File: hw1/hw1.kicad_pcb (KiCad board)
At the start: 2 copper layers, 68.6 x 53.3 mm, 28 parts, among them J1 CONN_01X06, P1 Power, P10 CONTROL, P2 Analog, P3 Digital, P4 Digital, P5 CONN_01X01, P6 CONN_01X01, P7 CONN_01X01, P8 CONN_01X01, P9 FX2LA, U1 STM32L151C6TxA, U2 MIC550x-3.3YM5, Y1 Crystal_GND24_Small

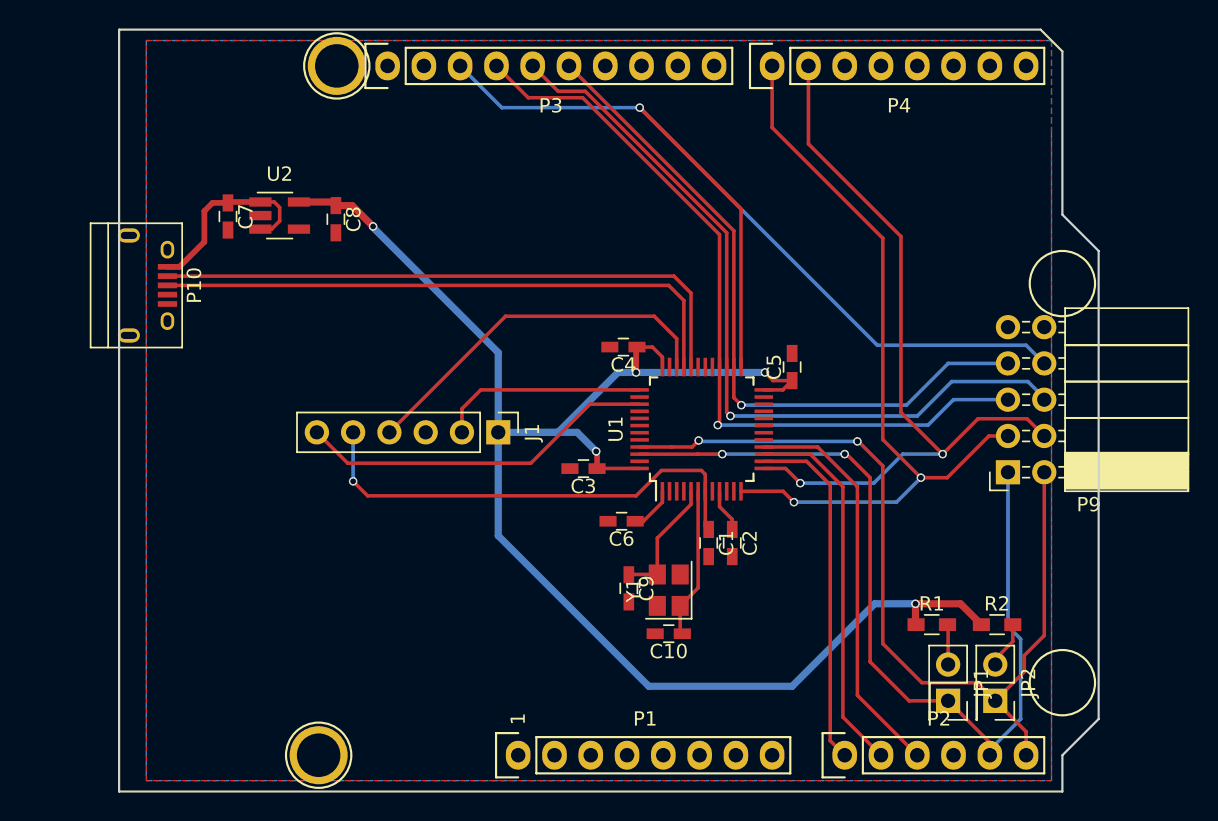
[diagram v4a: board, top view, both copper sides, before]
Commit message: "fix" grounds by tracks into pour
"finish" routing, ignore DRC violations from disconnected usb shield on
pin 6.

Add boot0 jumper pad "just in case" but really kinda dumb, we've got a
debug header on it. Why bother with this?

Change paper size in schema to get more space.

TODO: add silk?
TODO: replace "arduino" shape with just the pinpoints.
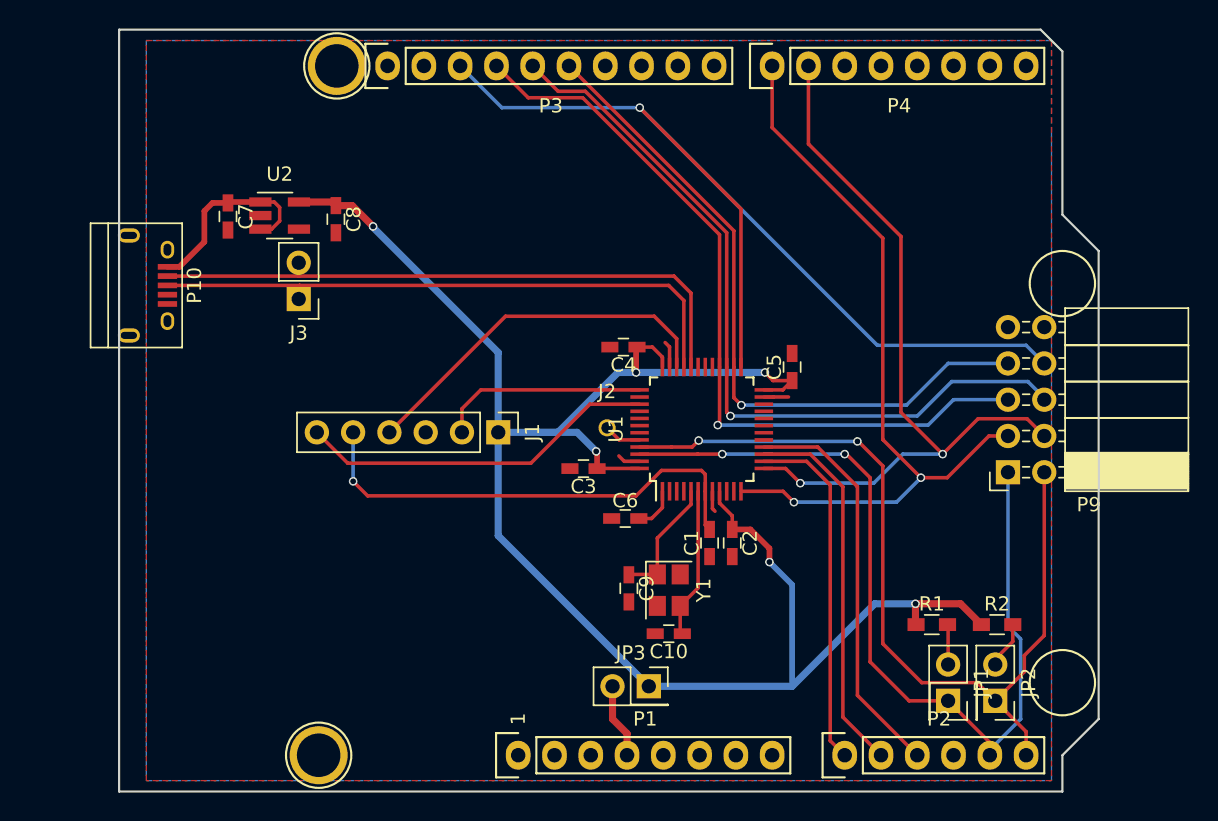
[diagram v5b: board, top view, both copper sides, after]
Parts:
- added J2: CONN_01X01_MALE, Wire_Pads:SolderWirePad_single_0-8mmDrill, F.Cu at (145.2, 100.9)
- added J3: CONN_01X02, Pin_Headers:Pin_Header_Straight_1x02_Pitch2.54mm, F.Cu at (123.6, 91.9)
- added JP3: Jumper_NC_Small, Socket_Strips:Socket_Strip_Straight_2x01_Pitch2.54mm, F.Cu at (148.1, 119.0)
- moved C6 0.32 mm to (146.4, 107.3), turned to 0 degrees
- moved C1 0.06 mm to (152.3, 109.0), turned to 90 degrees
- turned Y1 to 270 degrees
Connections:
- C1 pad 1: /NRST -> GND
- C1 pad 2: GND -> /NRST
- C6 pad 1: /VLCD -> GND
- C6 pad 2: GND -> /VLCD
- P1 pad 4: +3V3 -> Net-(JP3-Pad2)
- P1 pad 5: +5V -> (no net)
- P3 pad 10: /I2C_SCL -> (no net)
- P3 pad 9: /I2C_SDA -> (no net)
- U1 pad 44: (no net) -> Net-(J2-Pad1)
- Y1 pad 1: Net-(C10-Pad1) -> Net-(C9-Pad1)
- Y1 pad 3: Net-(C9-Pad1) -> Net-(C10-Pad1)
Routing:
- net +3V3: track 115.7 -> 129.2 mm, vias 5 -> 6
- net GND: track 0.00 -> 6.65 mm
- net Net-(JP3-Pad2): track 0.00 -> 5.25 mm
- net Net-(J2-Pad1): track 0.00 -> 2.62 mm
- net /USB_DP: track 41.3 -> 42.2 mm
- net /USB_DM: track 42.3 -> 43.3 mm

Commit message: hw1: drop arduinno style holes and board shape
More to go, nno need for the silk and dead shapes, we just needed the
pin spacings
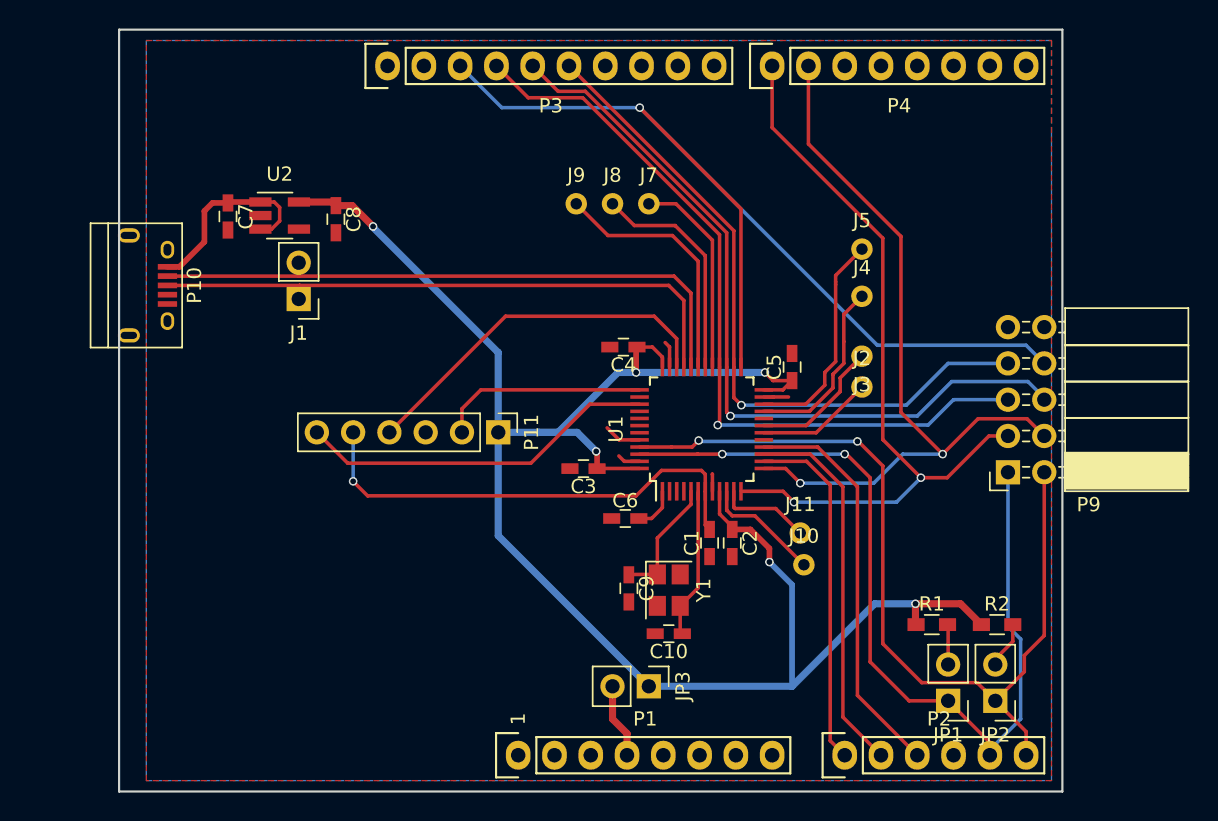
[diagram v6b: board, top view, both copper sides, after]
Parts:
- removed P5, P6, P7, P8: CONN_01X01, Socket_Arduino_Uno:Arduino_1pin
- added J10: TEST_1P, Measurement_Points:Measurement_Point_Round-TH_Small, F.Cu at (158.9, 110.5)
- added J11: TEST_1P, Measurement_Points:Measurement_Point_Round-TH_Small, F.Cu at (158.7, 108.3)
- added J4: TEST_1P, Measurement_Points:Measurement_Point_Round-TH_Small, F.Cu at (163.0, 91.7)
- added J5: TEST_1P, Measurement_Points:Measurement_Point_Round-TH_Small, F.Cu at (163.0, 88.4)
- added J7: TEST_1P, Measurement_Points:Measurement_Point_Round-TH_Small, F.Cu at (148.1, 85.2)
- added J8: TEST_1P, Measurement_Points:Measurement_Point_Round-TH_Small, F.Cu at (145.5, 85.2)
- added J9: TEST_1P, Measurement_Points:Measurement_Point_Round-TH_Small, F.Cu at (143.0, 85.2)
- added P11: CONN_01X06, Socket_Strips:Socket_Strip_Straight_1x06_Pitch2.54mm, F.Cu at (137.5, 101.2)
- J1: value CONN_01X06 -> CONN_01X02; footprint Pin_Headers:Pin_Header_Straight_1x06_Pitch2.54mm -> Pin_Headers:Pin_Header_Straight_1x02_Pitch2.54mm
- J2: value CONN_01X01_MALE -> TEST_1P; footprint Wire_Pads:SolderWirePad_single_0-8mmDrill -> Measurement_Points:Measurement_Point_Round-TH_Small
- J3: value CONN_01X02 -> TEST_1P; footprint Pin_Headers:Pin_Header_Straight_1x02_Pitch2.54mm -> Measurement_Points:Measurement_Point_Round-TH_Small
- JP1, JP2, JP3: footprint Socket_Strips:Socket_Strip_Straight_2x01_Pitch2.54mm -> Pin_Headers:Pin_Header_Straight_1x02_Pitch2.54mm
- moved J3 39.6 mm to (163.0, 95.9)
- moved J2 18.1 mm to (163.0, 98.0)
- moved J1 16.8 mm to (123.6, 91.9), turned to 180 degrees
- turned JP1 to 180 degrees
- turned JP2 to 180 degrees
- turned JP3 to 270 degrees
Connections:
- J1 pad 1: +3V3 -> /USB_DP
- J1 pad 2: /SWCLK -> /USB_DM
- J3 pad 1: /USB_DP -> Net-(J3-Pad1)
- U1 pad 10: (no net) -> Net-(J10-Pad1)
- U1 pad 11: (no net) -> Net-(J11-Pad1)
- U1 pad 18: (no net) -> Net-(J2-Pad1)
- U1 pad 19: (no net) -> Net-(J3-Pad1)
- U1 pad 21: (no net) -> Net-(J4-Pad1)
- U1 pad 22: (no net) -> Net-(J5-Pad1)
- U1 pad 29: (no net) -> Net-(J7-Pad1)
- U1 pad 30: (no net) -> Net-(J8-Pad1)
- U1 pad 31: (no net) -> Net-(J9-Pad1)
- U1 pad 44: Net-(J2-Pad1) -> GND
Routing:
- net Net-(J9-Pad1): track 0.00 -> 17.6 mm
- net Net-(J8-Pad1): track 0.00 -> 15.8 mm
- net Net-(J5-Pad1): track 0.00 -> 15.4 mm
- net Net-(J7-Pad1): track 0.00 -> 14.4 mm
- net Net-(J4-Pad1): track 0.00 -> 12.8 mm
- net Net-(J3-Pad1): track 0.00 -> 9.44 mm
- net Net-(J10-Pad1): track 0.00 -> 8.31 mm
- net Net-(J11-Pad1): track 0.00 -> 6.52 mm
- net Net-(J2-Pad1): track 2.62 -> 8.20 mm
- net GND: track 6.65 -> 9.01 mm
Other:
- board size 68.6 x 53.3 mm -> 66 x 53.3 mm

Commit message: hw1: shrinking after dropping arduino stuff
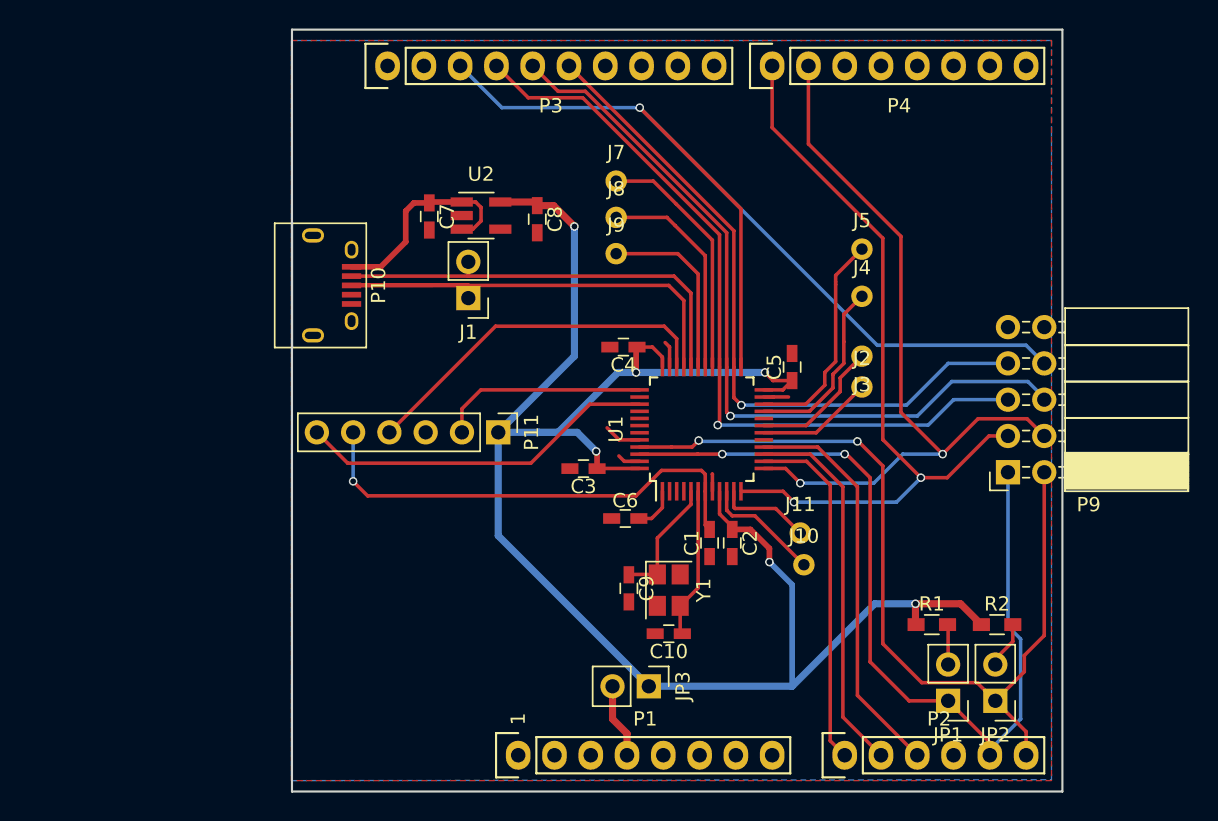
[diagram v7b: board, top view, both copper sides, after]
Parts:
- moved C7 14.1 mm to (132.7, 86.1)
- moved C8 14.1 mm to (140.3, 86.3)
- moved U2 14.1 mm to (136.3, 86.0)
- moved P10 12.9 mm to (125.9, 90.9)
- moved J1 11.9 mm to (135.4, 91.8)
- moved J9 4.47 mm to (145.8, 88.7)
- moved J7 2.78 mm to (145.8, 83.6)
- moved J8 0.99 mm to (145.8, 86.2)
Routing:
- net /USB_DM: track 43.3 -> 30.0 mm
- net Net-(J9-Pad1): track 17.6 -> 12.8 mm
- net /USB_DP: track 42.2 -> 45.6 mm
- net Net-(J7-Pad1): track 14.4 -> 17.3 mm
- net +3V3: track 129.2 -> 127.8 mm
- net +5V: track 13.7 -> 14.9 mm
- net Net-(J8-Pad1): track 15.8 -> 15.1 mm
- net /SWDIO: track 26.1 -> 25.5 mm
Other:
- board size 66 x 53.3 mm -> 53.9 x 53.3 mm
